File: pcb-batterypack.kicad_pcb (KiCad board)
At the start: 4 copper layers, 90 x 52 mm, 16 parts, among them J1 BATT_CON, J2 246, J3 246

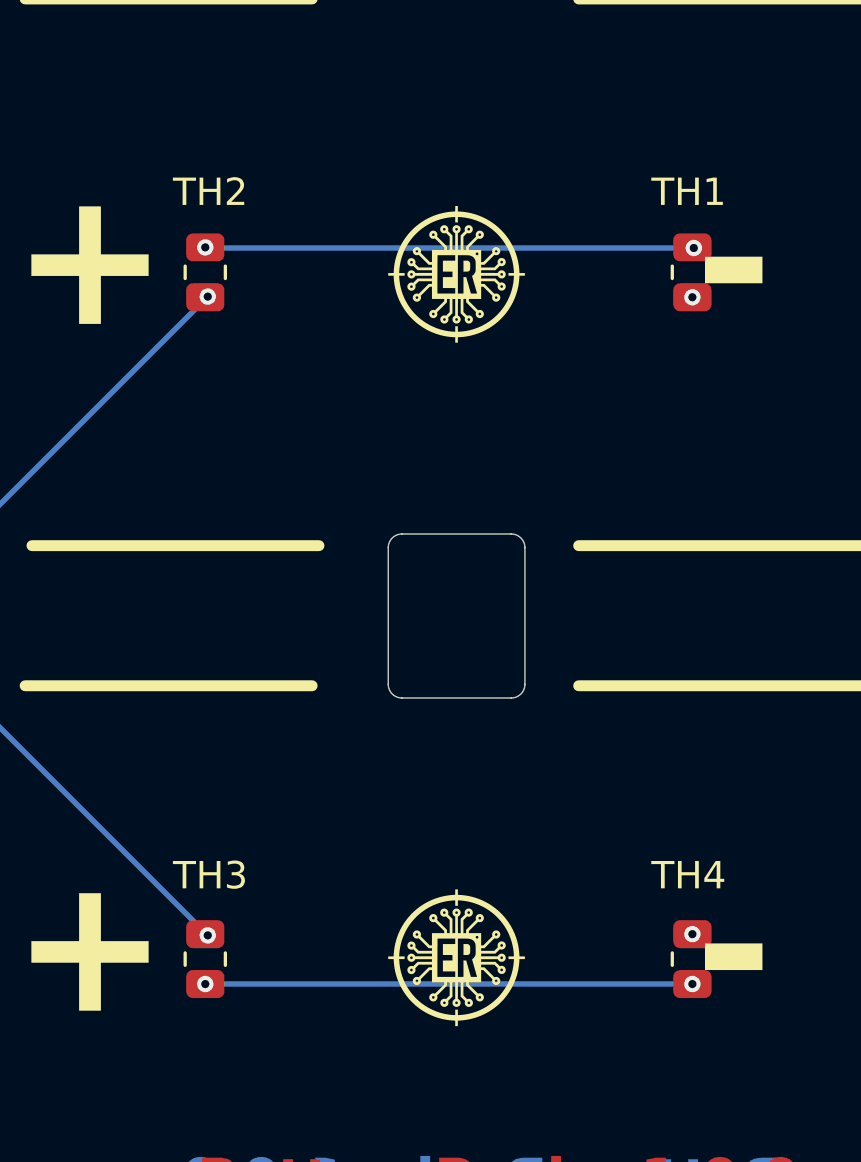
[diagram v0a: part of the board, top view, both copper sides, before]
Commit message: fix NTC location and thermal reliefs
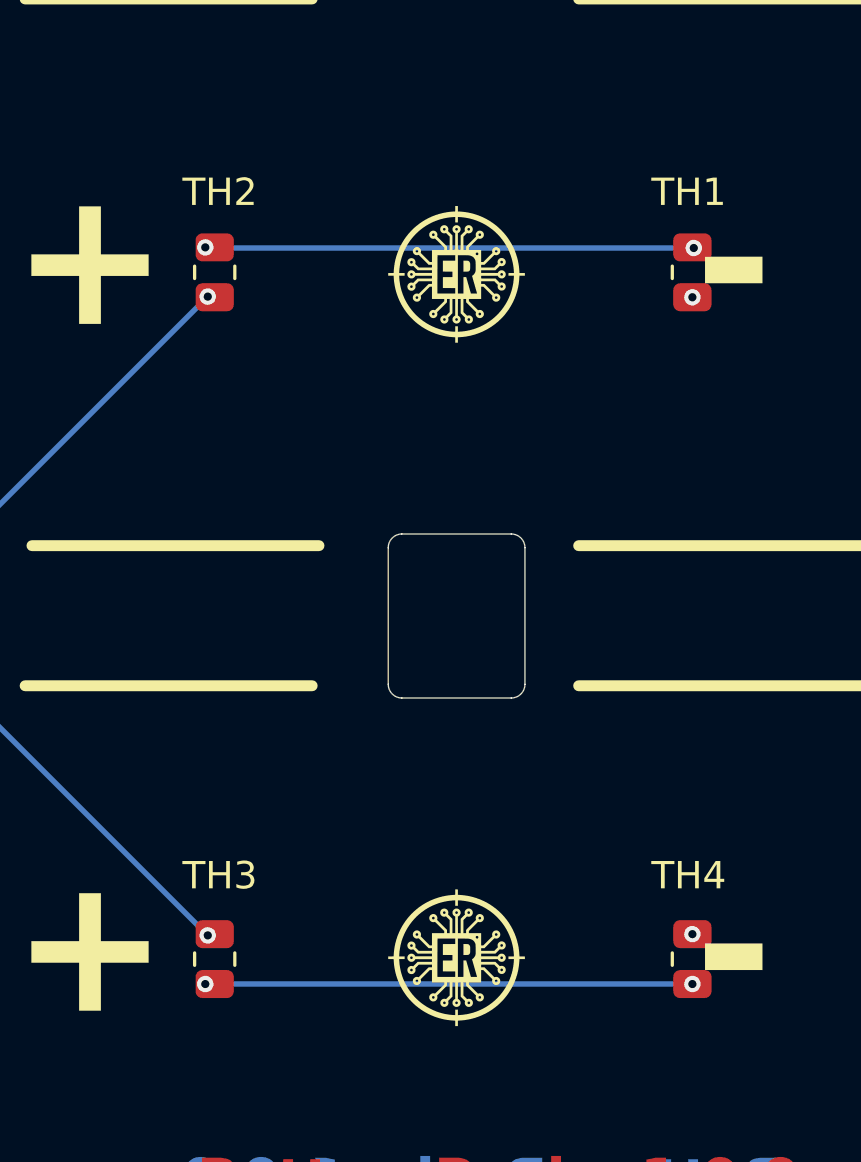
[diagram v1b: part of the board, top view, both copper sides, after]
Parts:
- moved TH2 0.35 mm to (151.1, 49.7)
- moved TH3 0.35 mm to (151.1, 74.8)
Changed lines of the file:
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@@
 	(footprint "Resistor_SMD:R_0805_2012Metric"
 		(layer "F.Cu")
-		(at 150.781 74.782 -90)
+		(at 151.126401 74.782 -90)
 		(descr "Resistor SMD 0805 (2012 Metric), square (rectangular) end terminal, IPC_7351 nominal, (Body size source: IPC-SM-782 page 72, https://www.pcb-3d.com/wordpress/wp-content/uploads/ipc-sm-782a_amendment_1_and_2.pdf), generated with kicad-footprint-generator")
 		(tags "resistor")
@@
 	(footprint "Resistor_SMD:R_0805_2012Metric"
 		(layer "F.Cu")
-		(at 150.781 49.657 90)
+		(at 151.126401 49.657 90)
 		(descr "Resistor SMD 0805 (2012 Metric), square (rectangular) end terminal, IPC_7351 nominal, (Body size source: IPC-SM-782 page 72, https://www.pcb-3d.com/wordpress/wp-content/uploads/ipc-sm-782a_amendment_1_and_2.pdf), generated with kicad-footprint-generator")
 		(tags "resistor")
@@
 			(net 2 "GND")
 			(pintype "passive")
+			(zone_connect 1)
+			(thermal_bridge_width 0.2)
+			(thermal_gap 0.2)
 		)
 		(model "${KICAD8_3DMODEL_DIR}/Resistor_SMD.3dshapes/R_0805_2012Metric.wrl"
@@
 			(net 2 "GND")
 			(pintype "passive")
+			(zone_connect 1)
+			(thermal_bridge_width 0.2)
+			(thermal_gap 0.2)
 		)
 		(model "${KICAD8_3DMODEL_DIR}/Resistor_SMD.3dshapes/R_0805_2012Metric.wrl"
@@
 		(at 159.971401 49.73)
 		(property "Reference" "G***"
-			(at 0 0 360)
+			(at 0 0 0)
 			(layer "F.SilkS")
 			(hide yes)
@@
 		)
 		(property "Value" "LOGO"
-			(at 0.75 0 360)
+			(at 0.75 0 0)
 			(layer "F.SilkS")
 			(hide yes)
@@
 	)
 	(segment
-		(start 150.781 50.5695)
-		(end 150.848901 50.5695)
+		(start 151.126401 73.8695)
+		(end 151.081901 73.914)
 		(width 0.2)
 		(layer "F.Cu")
@@
 	)
 	(segment
-		(start 150.827901 73.8695)
-		(end 150.872401 73.914)
+		(start 151.102901 50.546)
+		(end 150.872401 50.546)
 		(width 0.2)
 		(layer "F.Cu")
@@
 	)
 	(segment
-		(start 150.848901 50.5695)
-		(end 150.872401 50.546)
+		(start 151.126401 50.5695)
+		(end 151.102901 50.546)
 		(width 0.2)
 		(layer "F.Cu")
@@
 	)
 	(segment
-		(start 150.781 73.8695)
-		(end 150.827901 73.8695)
+		(start 151.081901 73.914)
+		(end 150.872401 73.914)
 		(width 0.2)
 		(layer "F.Cu")
@@
 	(segment
 		(start 168.652401 48.768)
-		(end 150.8045 48.768)
+		(end 150.895901 48.768)
 		(width 0.2)
 		(layer "B.Cu")
@@
 	)
 	(segment
-		(start 150.8045 48.768)
-		(end 150.781 48.7445)
+		(start 150.895901 48.768)
+		(end 150.872401 48.7445)
 		(width 0.2)
 		(layer "B.Cu")
@@
 	)
 	(segment
-		(start 168.601 75.6945)
-		(end 168.5985 75.692)
+		(start 150.874901 75.692)
+		(end 150.872401 75.6945)
 		(width 0.2)
 		(layer "B.Cu")
@@
 	)
 	(segment
-		(start 150.7835 75.692)
-		(end 150.781 75.6945)
+		(start 168.5985 75.692)
+		(end 150.874901 75.692)
 		(width 0.2)
 		(layer "B.Cu")
@@
 	)
 	(segment
-		(start 168.5985 75.692)
-		(end 150.7835 75.692)
+		(start 168.601 75.6945)
+		(end 168.5985 75.692)
 		(width 0.2)
 		(layer "B.Cu")

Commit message: Bumping release from 1.0.0 to 1.0.1
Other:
- board text added: "BatteryPack v1.0.1"
- board text removed: "BatteryPack v1.0.0"
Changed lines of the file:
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@@
 		(layer "Edge.Cuts")
 	)
-	(gr_text "BatteryPack v1.0.0"
+	(gr_text "BatteryPack v1.0.1"
 		(at 150.471401 83.73 0)
 		(layer "F.Cu")
@@
 		)
 	)
-	(gr_text "BatteryPack v1.0.0"
+	(gr_text "BatteryPack v1.0.1"
 		(at 171.971401 83.73 -0)
 		(layer "B.Cu")

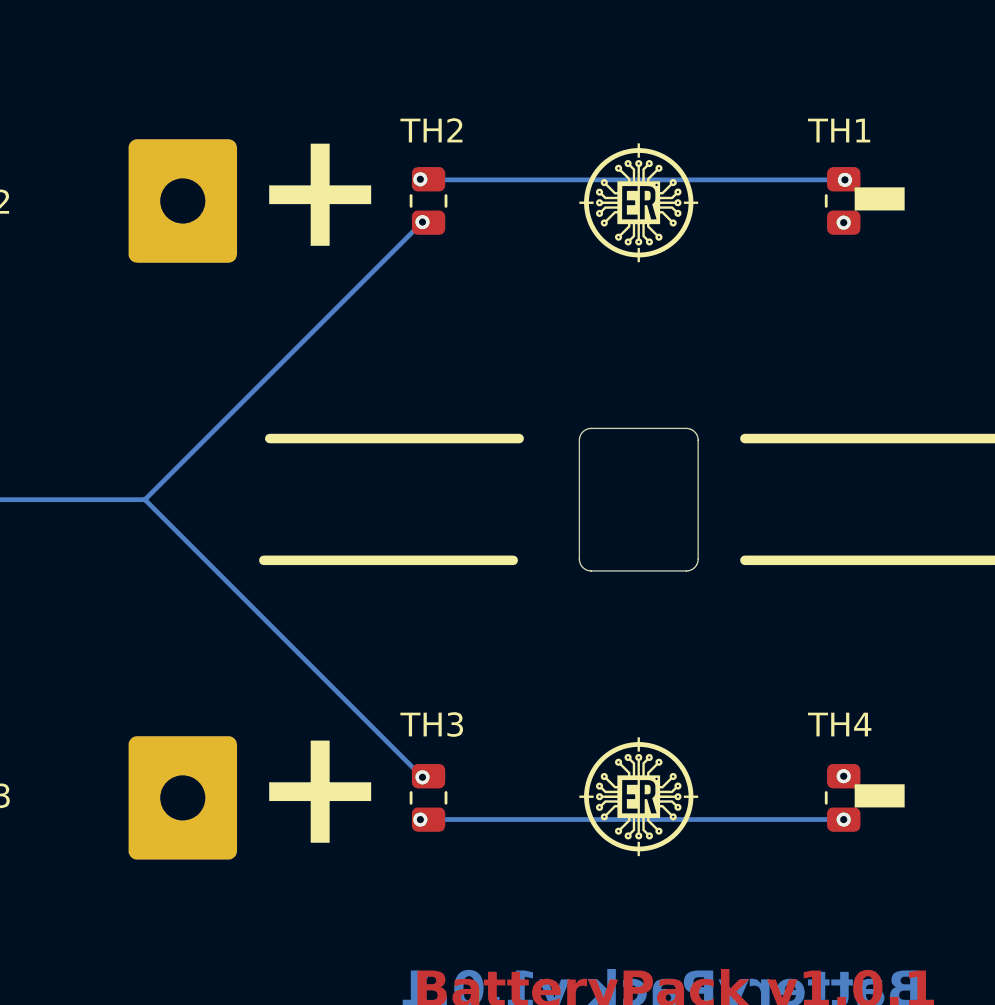
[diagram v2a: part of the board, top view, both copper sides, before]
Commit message: fix: no via in pad to reduce cost
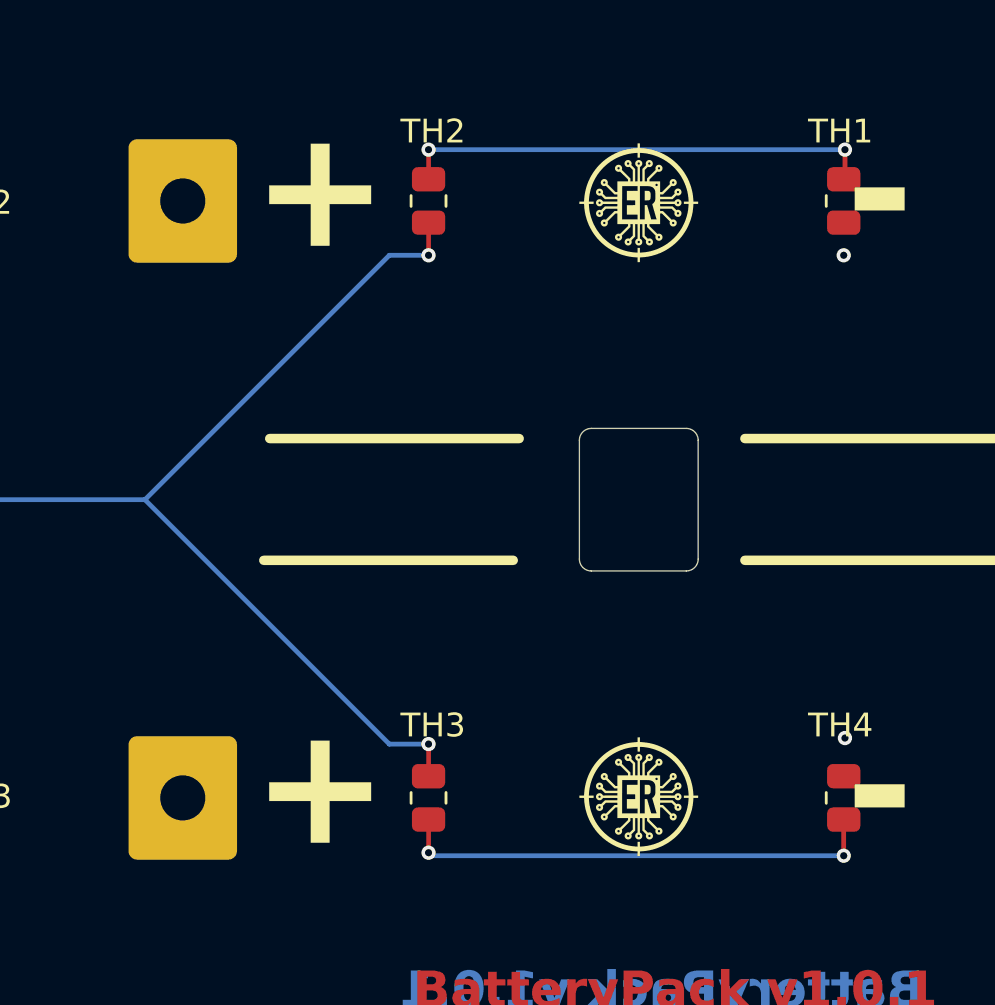
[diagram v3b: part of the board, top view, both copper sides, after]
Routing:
- net Net-(TH3-Pad2): track 17.7 -> 20.4 mm
- net Net-(TH1-Pad1): track 17.9 -> 20.0 mm
- net /NTC: track 55.3 -> 56.8 mm
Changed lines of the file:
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@@
 	)
 	(segment
-		(start 151.126401 73.8695)
-		(end 151.081901 73.914)
+		(start 151.126401 51.943)
+		(end 151.126401 50.5695)
 		(width 0.2)
 		(layer "F.Cu")
@@
 	)
 	(segment
-		(start 151.102901 50.546)
-		(end 150.872401 50.546)
-		(width 0.2)
-		(layer "F.Cu")
-		(net 1)
-	)
-	(segment
-		(start 151.126401 50.5695)
-		(end 151.102901 50.546)
-		(width 0.2)
-		(layer "F.Cu")
-		(net 1)
-	)
-	(segment
-		(start 151.081901 73.914)
-		(end 150.872401 73.914)
+		(start 151.126401 72.517)
+		(end 151.126401 73.8695)
 		(width 0.2)
 		(layer "F.Cu")
@@
 	)
 	(via
-		(at 150.872401 50.546)
+		(at 151.126401 51.943)
 		(size 0.6)
 		(drill 0.3)
@@
 	)
 	(via
-		(at 150.872401 73.914)
+		(at 151.126401 72.517)
 		(size 0.6)
 		(drill 0.3)
 		(layers "F.Cu" "B.Cu")
+		(net 1)
+	)
+	(segment
+		(start 149.475401 72.517)
+		(end 139.188401 62.23)
+		(width 0.2)
+		(layer "B.Cu")
 		(net 1)
 	)
@@
 	)
 	(segment
-		(start 150.872401 73.914)
+		(start 151.126401 51.943)
+		(end 149.475401 51.943)
+		(width 0.2)
+		(layer "B.Cu")
+		(net 1)
+	)
+	(segment
+		(start 149.475401 51.943)
 		(end 139.188401 62.23)
 		(width 0.2)
@@
 	)
 	(segment
-		(start 150.872401 50.546)
-		(end 139.188401 62.23)
+		(start 151.126401 72.517)
+		(end 149.475401 72.517)
 		(width 0.2)
 		(layer "B.Cu")
@@
 	)
 	(via
-		(at 168.601 73.8695)
+		(at 168.652401 72.263)
 		(size 0.6)
 		(drill 0.3)
@@
 	)
 	(via
-		(at 168.601 50.5695)
+		(at 168.601 51.943)
 		(size 0.6)
 		(drill 0.3)
@@
 	)
 	(segment
-		(start 168.601 48.7445)
-		(end 168.628901 48.7445)
+		(start 168.652401 47.498)
+		(end 168.652401 48.693099)
 		(width 0.2)
 		(layer "F.Cu")
@@
 	)
 	(segment
-		(start 168.628901 48.7445)
-		(end 168.652401 48.768)
+		(start 168.652401 48.693099)
+		(end 168.601 48.7445)
+		(width 0.2)
+		(layer "F.Cu")
+		(net 3)
+	)
+	(segment
+		(start 151.126401 47.498)
+		(end 151.126401 48.7445)
 		(width 0.2)
 		(layer "F.Cu")
@@
 	)
 	(via
-		(at 150.781 48.7445)
+		(at 151.126401 47.498)
 		(size 0.6)
 		(drill 0.3)
@@
 	)
 	(via
-		(at 168.652401 48.768)
+		(at 168.652401 47.498)
 		(size 0.6)
 		(drill 0.3)
@@
 	)
 	(segment
-		(start 168.652401 48.768)
-		(end 150.895901 48.768)
+		(start 168.652401 47.498)
+		(end 151.126401 47.498)
 		(width 0.2)
 		(layer "B.Cu")
@@
 	)
 	(segment
-		(start 150.895901 48.768)
-		(end 150.872401 48.7445)
+		(start 151.126401 77.089)
+		(end 151.126401 75.6945)
 		(width 0.2)
-		(layer "B.Cu")
-		(net 3)
+		(layer "F.Cu")
+		(net 4)
+	)
+	(segment
+		(start 168.601 77.216)
+		(end 168.601 75.6945)
+		(width 0.2)
+		(layer "F.Cu")
+		(net 4)
 	)
 	(via
-		(at 150.781 75.6945)
+		(at 151.126401 77.089)
 		(size 0.6)
 		(drill 0.3)
@@
 	)
 	(via
-		(at 168.601 75.6945)
+		(at 168.601 77.216)
 		(size 0.6)
 		(drill 0.3)
@@
 	)
 	(segment
-		(start 150.874901 75.692)
-		(end 150.872401 75.6945)
+		(start 168.601 77.216)
+		(end 151.253401 77.216)
 		(width 0.2)
 		(layer "B.Cu")
@@
 	)
 	(segment
-		(start 168.5985 75.692)
-		(end 150.874901 75.692)
+		(start 151.253401 77.216)
+		(end 151.126401 77.089)
 		(width 0.2)
 		(layer "B.Cu")
-		(net 4)
-	)
-	(segment
-		(start 168.601 75.6945)
-		(end 168.5985 75.692)
-		(width 0.2)
-		(layer "B.Cu")

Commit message: Bumping release from 1.0.1 to 1.0.2
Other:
- board text added: "BatteryPack v1.0.2"
- board text removed: "BatteryPack v1.0.1"
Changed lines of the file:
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@@
 		(layer "Edge.Cuts")
 	)
-	(gr_text "BatteryPack v1.0.1"
+	(gr_text "BatteryPack v1.0.2"
 		(at 150.471401 83.73 0)
 		(layer "F.Cu")
@@
 		)
 	)
-	(gr_text "BatteryPack v1.0.1"
+	(gr_text "BatteryPack v1.0.2"
 		(at 171.971401 83.73 -0)
 		(layer "B.Cu")

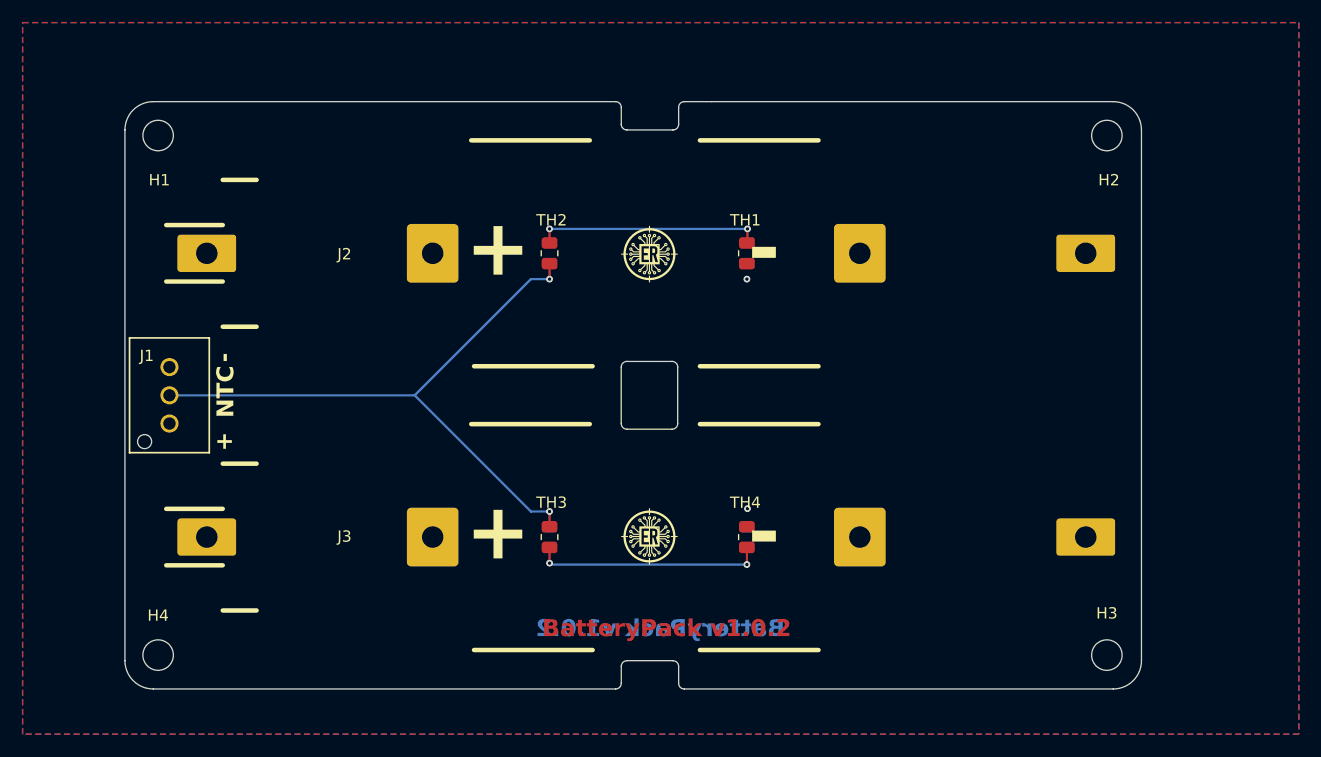
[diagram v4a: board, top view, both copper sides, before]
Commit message: refactor battery pack edge cuts outline
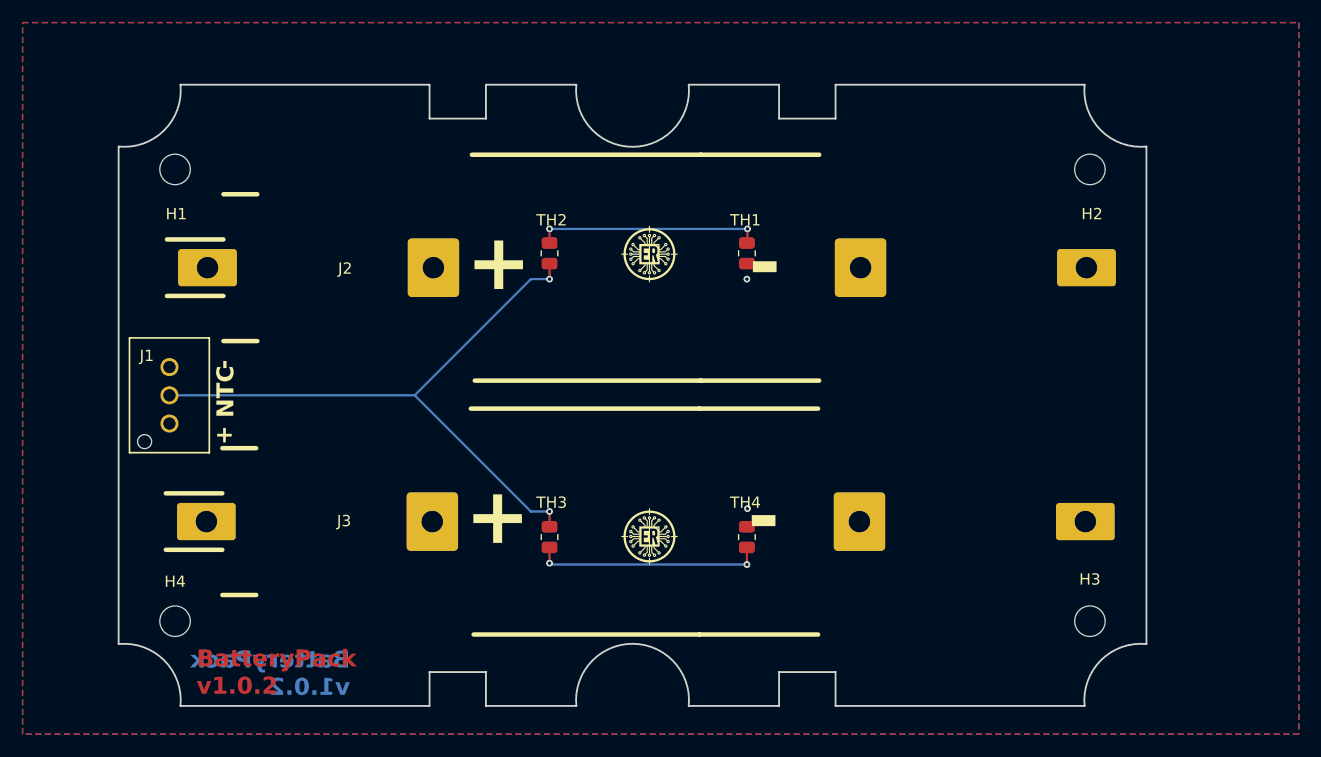
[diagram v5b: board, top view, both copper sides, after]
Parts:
- moved H1 3.35 mm to (118.0, 42.2)
- moved H2 3.35 mm to (199.0, 42.2)
- moved H3 3.35 mm to (199.0, 82.2)
- moved H4 3.35 mm to (118.0, 82.2)
- moved J3 1.37 mm to (159.7, 73.4)
- moved J2 1.27 mm to (159.8, 50.9)
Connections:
- J1 pad 1: /BATP -> GND
- J1 pad 3: GND -> /BATP
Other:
- board size 90 x 52 mm -> 91 x 55 mm

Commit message: modified edge cuts geometry
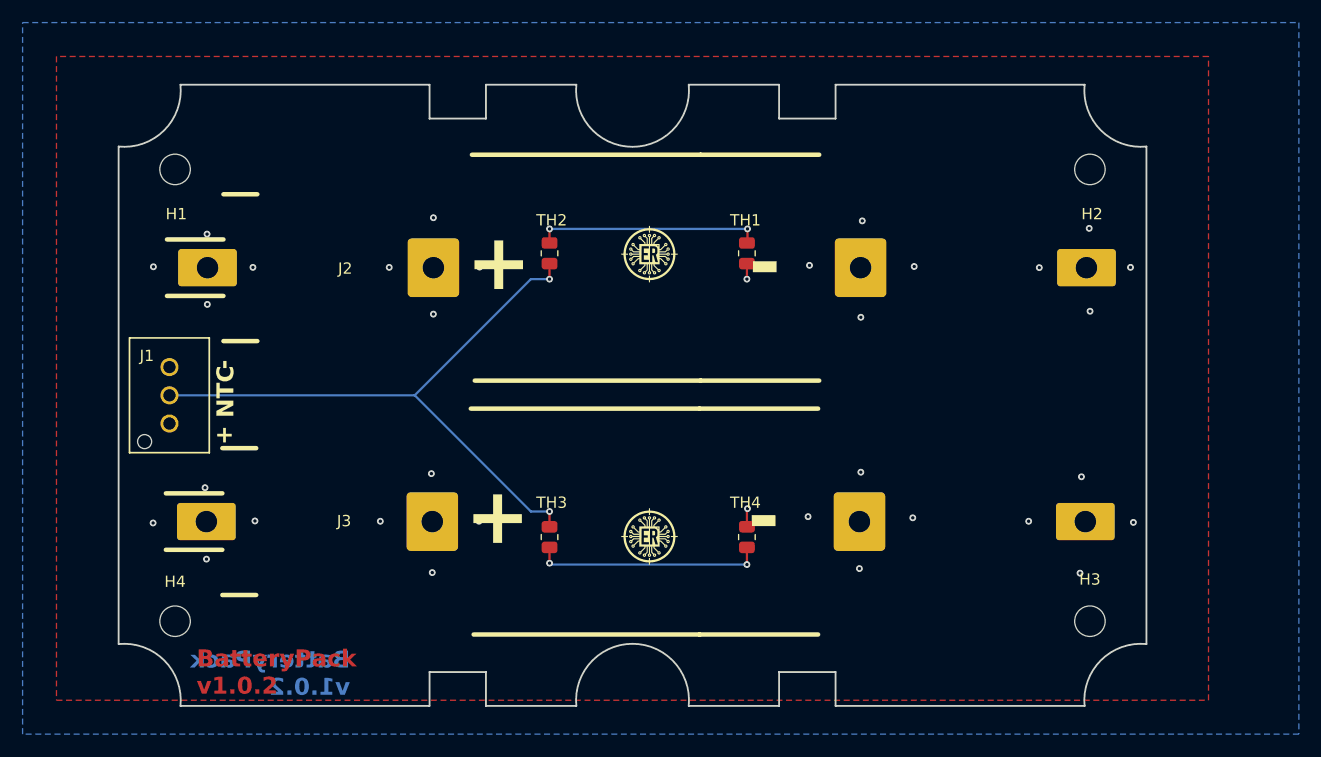
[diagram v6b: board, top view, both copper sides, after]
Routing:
- net GND: track 0.00 -> 3.00 mm, vias 2 -> 18
- net /BATP: vias 0 -> 16
- added copper zone on F.Cu, net /BATP
- added copper zone on In1.Cu, net GND
- removed copper zone on In1.Cu, net /BATP
- removed copper zone on F.Cu, net GND
